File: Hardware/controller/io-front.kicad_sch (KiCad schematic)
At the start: 20 parts

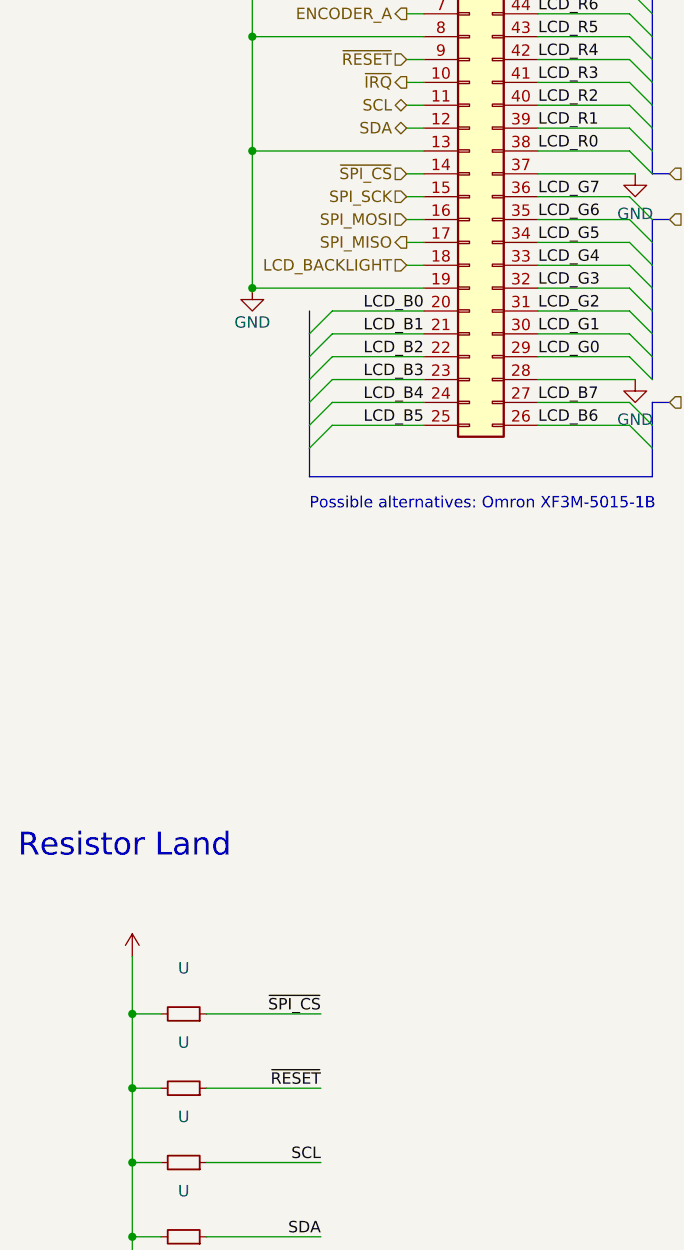
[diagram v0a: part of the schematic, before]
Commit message: hw: start working on rev4 controller
- removed SPI for display, and the associated SPI mux nonsense, and any
  superfluous resistors for pull-ups

- removed MAC address EEPROM

- start adding i2c RTC (which will also contain EEPROM with the MAC of
  the system, lol)

- start moving some components from bottom to top side of board

- tweaked positions of some mains voltage traces

- increased values of power indicator LED's current dropping resistors

- take 3V3 from SoM rather than generate it ourselves
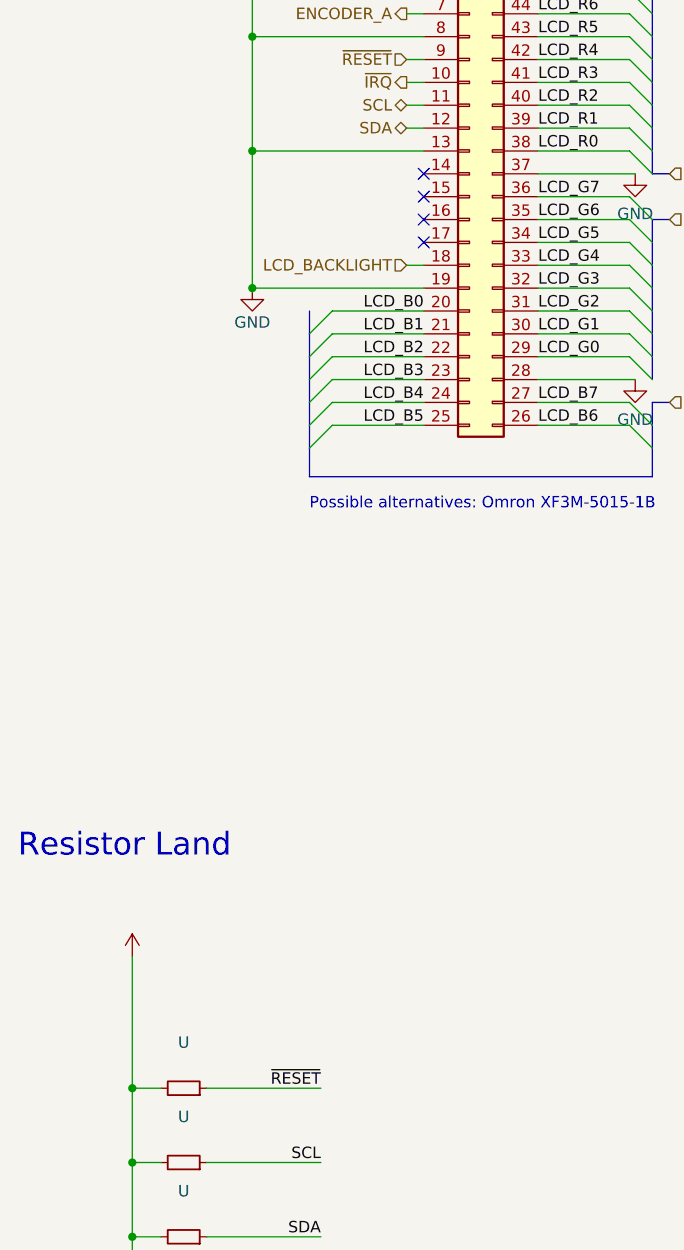
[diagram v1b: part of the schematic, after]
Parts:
- removed U: (no value), symbol Device:R_Small
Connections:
- net SPI_MISO: no longer names the net of J.17 (Pin_17)
- net SPI_MOSI: no longer names the net of J.16 (Pin_16)
- net SPI_SCK: no longer names the net of J.15 (Pin_15)
- net ~{SPI_CS}: no longer names the net of J.14 (Pin_14)
- no-connect marks 1 -> 5
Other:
- title: (none) -> Programmable Load Controller
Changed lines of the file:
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@@
 (kicad_sch (version 20220404) (generator eeschema)
   (paper "A4")
+  (title_block
+    (title "Programmable Load Controller")
+    (date "2022-06-28")
+    (rev "4")
+  )
   (junction (at 64.135 35.56) (diameter 0) (color 0 0 0 0)
   )
-  (junction (at 31.75 156.845) (diameter 0) (color 0 0 0 0)
-  )
   (junction (at 36.83 35.56) (diameter 0) (color 0 0 0 0)
   )
@@
   (junction (at 31.75 181.61) (diameter 0) (color 0 0 0 0)
   )
+  (no_connect (at 64.135 66.04))
   (no_connect (at 129.54 46.99))
+  (no_connect (at 64.135 68.58))
+  (no_connect (at 64.135 63.5))
+  (no_connect (at 64.135 71.12))
   (bus_entry (at 89.535 86.36) (size -2.54 -2.54)
     (stroke (width 0) (type default))
@@
     (stroke (width 0) (type default))
   )
-  (wire (pts (xy 62.23 71.12) (xy 64.135 71.12))
-    (stroke (width 0) (type default))
-  )
   (wire (pts (xy 62.23 50.8) (xy 64.135 50.8))
     (stroke (width 0) (type default))
@@
     (stroke (width 0) (type default))
   )
-  (wire (pts (xy 62.23 68.58) (xy 64.135 68.58))
-    (stroke (width 0) (type default))
-  )
   (wire (pts (xy 86.995 66.04) (xy 76.835 66.04))
     (stroke (width 0) (type default))
@@
     (stroke (width 0) (type default))
   )
-  (wire (pts (xy 40.005 156.845) (xy 52.705 156.845))
-    (stroke (width 0) (type default))
-  )
   (bus (pts (xy 89.535 63.5) (xy 91.44 63.5))
     (stroke (width 0) (type default))
@@
     (stroke (width 0) (type default))
   )
-  (wire (pts (xy 31.75 150.495) (xy 31.75 156.845))
-    (stroke (width 0) (type default))
-  )
   (bus (pts (xy 89.535 48.26) (xy 89.535 50.8))
     (stroke (width 0) (type default))
@@
     (stroke (width 0) (type default))
   )
-  (wire (pts (xy 31.75 156.845) (xy 31.75 165.1))
+  (wire (pts (xy 31.75 150.495) (xy 31.75 165.1))
     (stroke (width 0) (type default))
   )
@@
     (stroke (width 0) (type default))
   )
-  (wire (pts (xy 62.23 66.04) (xy 64.135 66.04))
-    (stroke (width 0) (type default))
-  )
   (wire (pts (xy 26.035 35.56) (xy 26.035 33.655))
     (stroke (width 0) (type default))
@@
     (stroke (width 0) (type default))
   )
-  (wire (pts (xy 62.23 63.5) (xy 64.135 63.5))
-    (stroke (width 0) (type default))
-  )
   (wire (pts (xy 184.15 36.83) (xy 185.42 36.83))
     (stroke (width 0) (type default))
@@
   )
   (wire (pts (xy 86.995 78.74) (xy 76.835 78.74))
-    (stroke (width 0) (type default))
-  )
-  (wire (pts (xy 31.75 156.845) (xy 34.925 156.845))
     (stroke (width 0) (type default))
   )
@@
     (effects (font (size 1.27 1.27)) (justify right bottom))
   )
-  (label "~{SPI_CS}" (at 52.705 156.845 0) (fields_autoplaced)
-    (effects (font (size 1.27 1.27)) (justify right bottom))
-  )
   (label "LCD_R6" (at 76.835 45.72 0) (fields_autoplaced)
     (effects (font (size 1.27 1.27)) (justify left bottom))
@@
     (effects (font (size 1.27 1.27)) (justify right))
   )
-  (hierarchical_label "SPI_SCK" (shape input) (at 62.23 66.04 180) (fields_autoplaced)
-    (effects (font (size 1.27 1.27)) (justify right))
-  )
   (hierarchical_label "ENCODER_A" (shape output) (at 62.23 45.72 180) (fields_autoplaced)
     (effects (font (size 1.27 1.27)) (justify right))
@@
     (effects (font (size 1.27 1.27)) (justify left))
   )
-  (hierarchical_label "SPI_MISO" (shape output) (at 62.23 71.12 180) (fields_autoplaced)
-    (effects (font (size 1.27 1.27)) (justify right))
-  )
   (hierarchical_label "LCD_R[0..7]" (shape input) (at 91.44 63.5 0) (fields_autoplaced)
     (effects (font (size 1.27 1.27)) (justify left))
@@
     (effects (font (size 1.27 1.27)) (justify left))
   )
-  (hierarchical_label "SPI_MOSI" (shape input) (at 62.23 68.58 180) (fields_autoplaced)
-    (effects (font (size 1.27 1.27)) (justify right))
-  )
   (hierarchical_label "LCD_B[0..7]" (shape input) (at 91.44 88.9 0) (fields_autoplaced)
     (effects (font (size 1.27 1.27)) (justify left))
-  )
-  (hierarchical_label "~{SPI_CS}" (shape input) (at 62.23 63.5 180) (fields_autoplaced)
-    (effects (font (size 1.27 1.27)) (justify right))
   )
   (hierarchical_label "SCL" (shape bidirectional) (at 62.23 55.88 180) (fields_autoplaced)
@@
       (effects (font (size 1.27 1.27)) hide)
     )
-    (pin "1")
-    (pin "2")
-  )
-  (symbol (lib_id "Device:R_Small") (at 37.465 156.845 270) (mirror x) (unit 1)
-    (in_bom yes) (on_board yes)
-    (default_instance (reference "U") (unit 1) (value "") (footprint ""))
-    (property "Reference" "U" (id 0) (at 37.465 151.765 90)
-      (effects (font (size 1.27 1.27)))
-    )
-    (property "Value" "" (id 1) (at 37.465 154.305 90)
-      (effects (font (size 1.27 1.27)))
-    )
-    (property "Footprint" "" (id 2) (at 37.465 156.845 0)
-      (effects (font (size 1.27 1.27)) hide)
-    )
-    (property "Datasheet" "~" (id 3) (at 37.465 156.845 0)
-      (effects (font (size 1.27 1.27)) hide)
-    )
-    (property "MPN" "" (id 4) (at 37.465 156.845 90)
-      (effects (font (size 1.27 1.27)) hide)
-    )

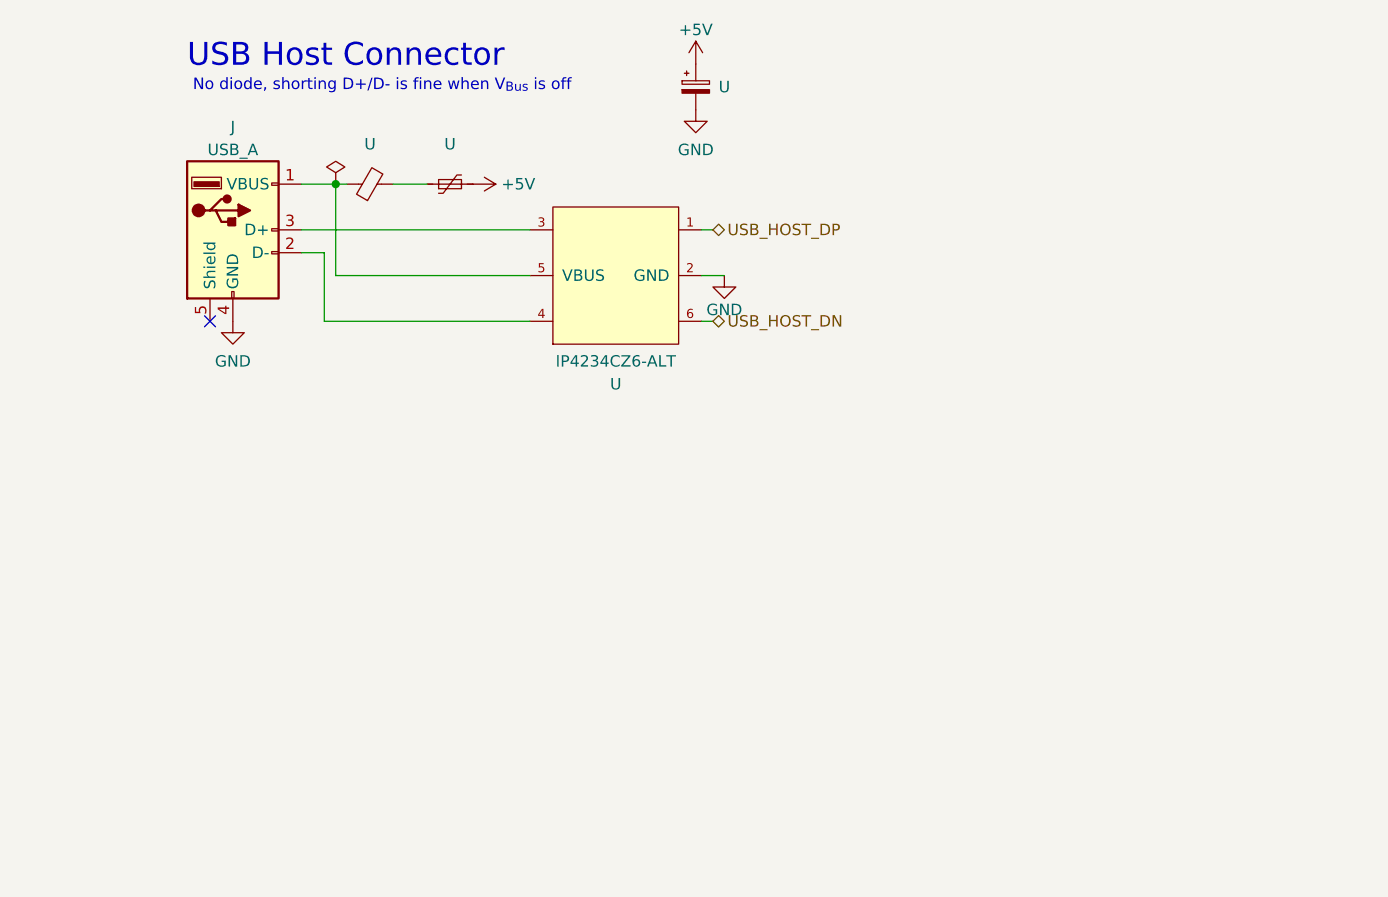
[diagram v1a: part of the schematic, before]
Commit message: hw: updates to usb host connector
- added a status indicator LED (including a lightpipe) next to the host
  connector

- start reworking the host connector power arrangement, using an actual
  USB power switch + current limiting IC (though we should revisit
  whether we'll use one without an error output)

- create footprint for AP22817 USB power switch
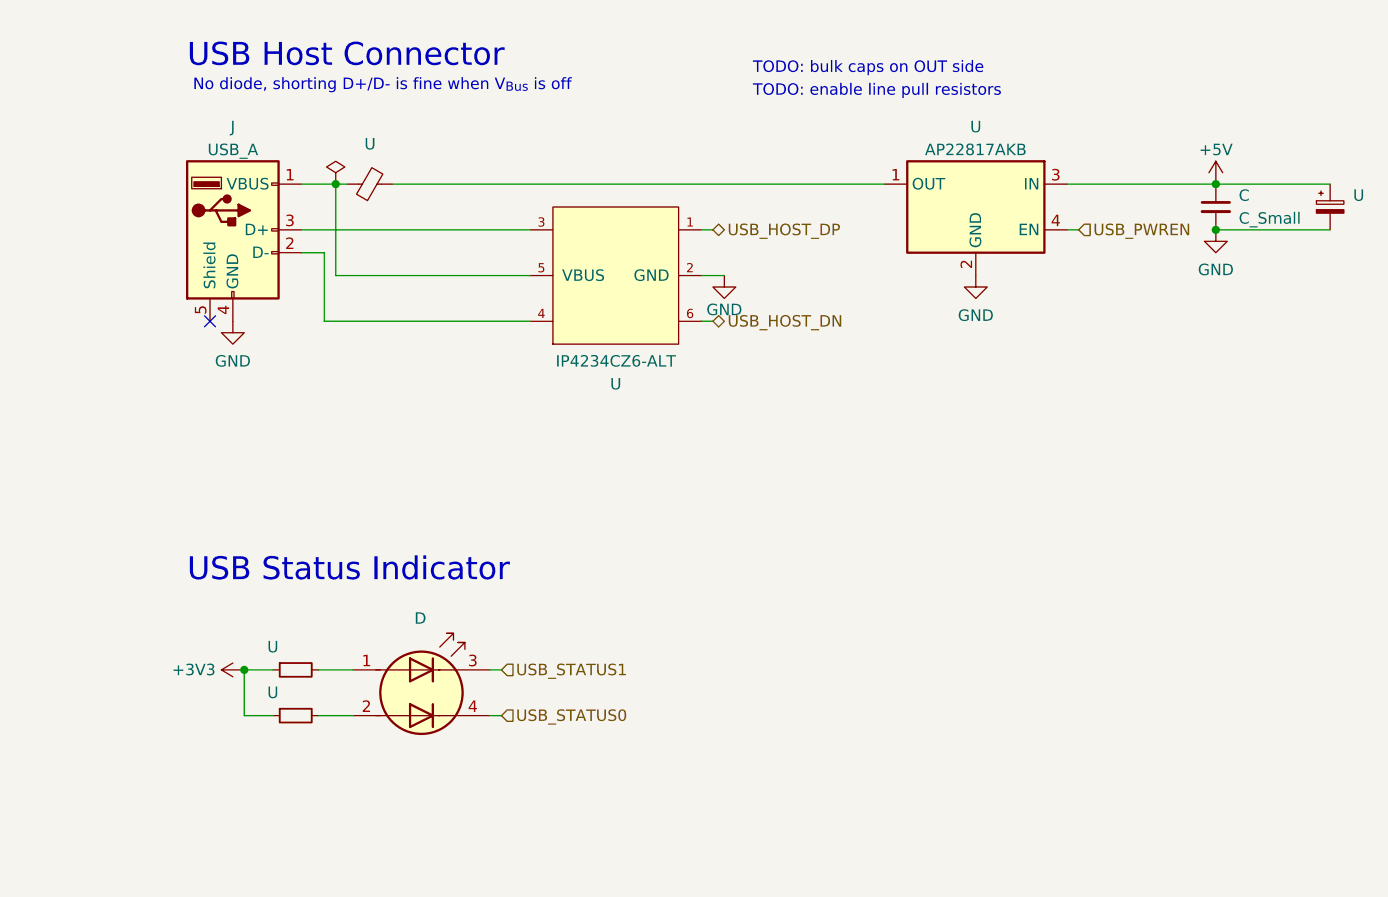
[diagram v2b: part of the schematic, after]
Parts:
- removed U: (no value), symbol Device:Polyfuse_Small
- added C: C_Small, symbol Device:C_Small
- added D: LED_Dual_AAKK, symbol Device:LED_Dual_AAKK
- added U (x2): (no value), symbol Device:R_Small
- added U: AP22817AKB, Package_SO:TSOP-5_1.65x3.05mm_P0.95mm, symbol programmable-load:AP22817AKB
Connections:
- net +3V3: now also U.1, U.1
- net +5V: now also C.1, U.3 (IN)
- net GND: now also C.2, U.2 (GND)
- net at U.2: now also U.1 (OUT), U.5 (OUT)
- new net: D.2 (A2), U.2
- new net: D.1 (A1), U.2
- new net USB_PWREN: U.4 (EN)
- new net USB_STATUS0: D.4 (K2)
- new net USB_STATUS1: D.3 (K1)
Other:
- note added: "TODO: bulk caps on OUT side"
- note added: "TODO: enable line pull resistors"
- note added: "USB Status Indicator"
- moved on the sheet: U

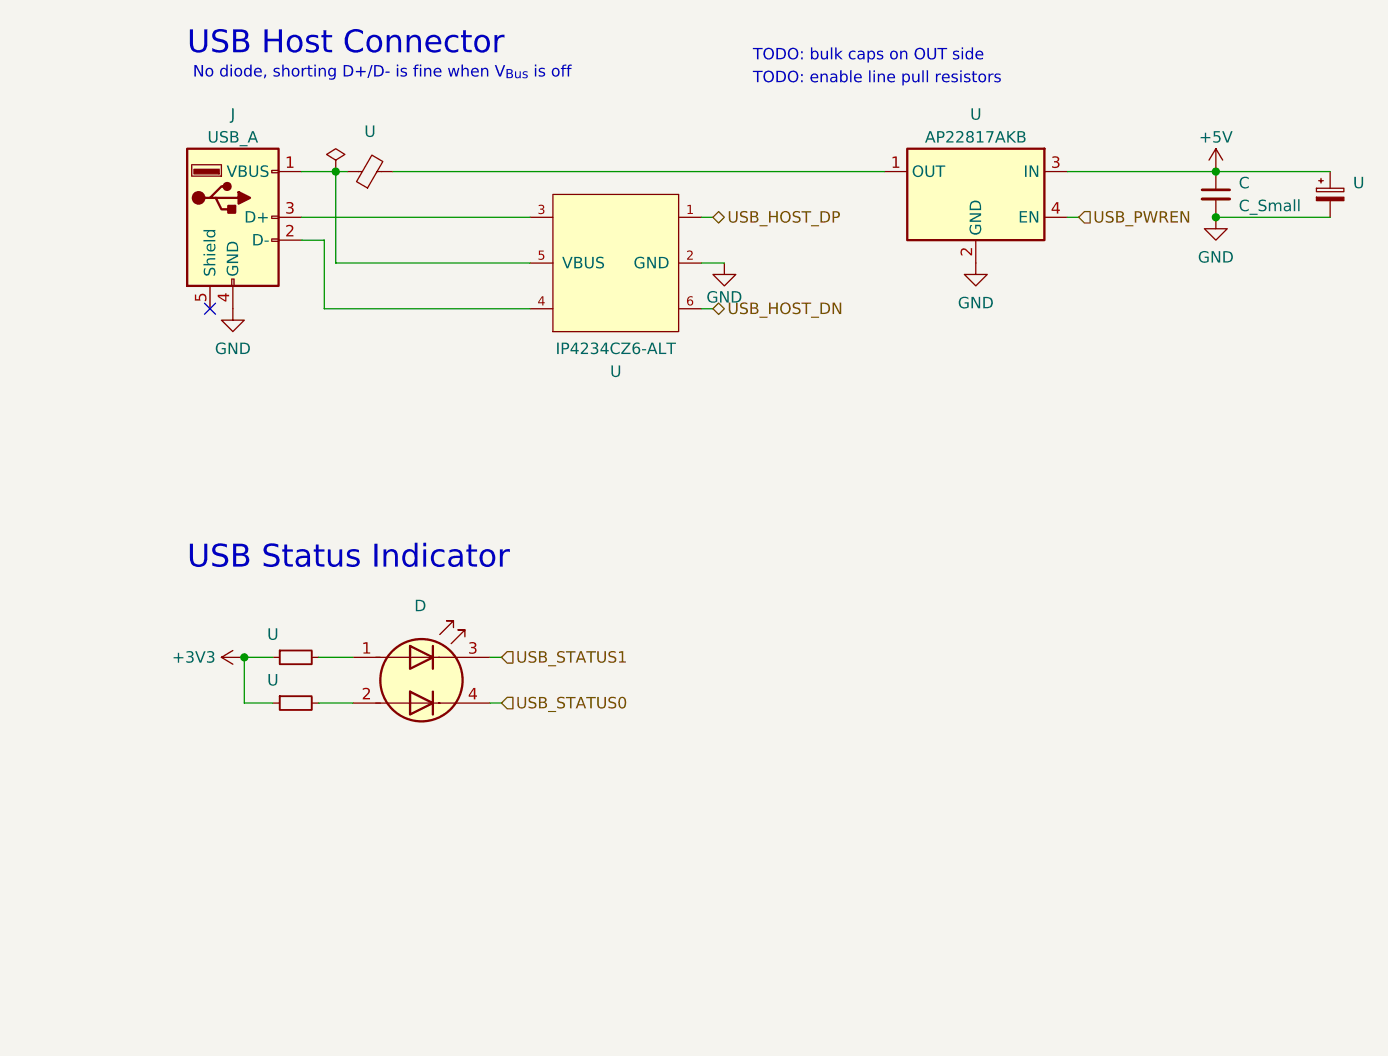
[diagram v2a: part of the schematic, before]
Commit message: hw: revise USB power stuff
- fixed the remaining usb powering stuff for the front panel host
  connector

- replaced 33µF SMD caps with through-hole equivalents

- removed some of the bottom mounted components for analog board power
  connection
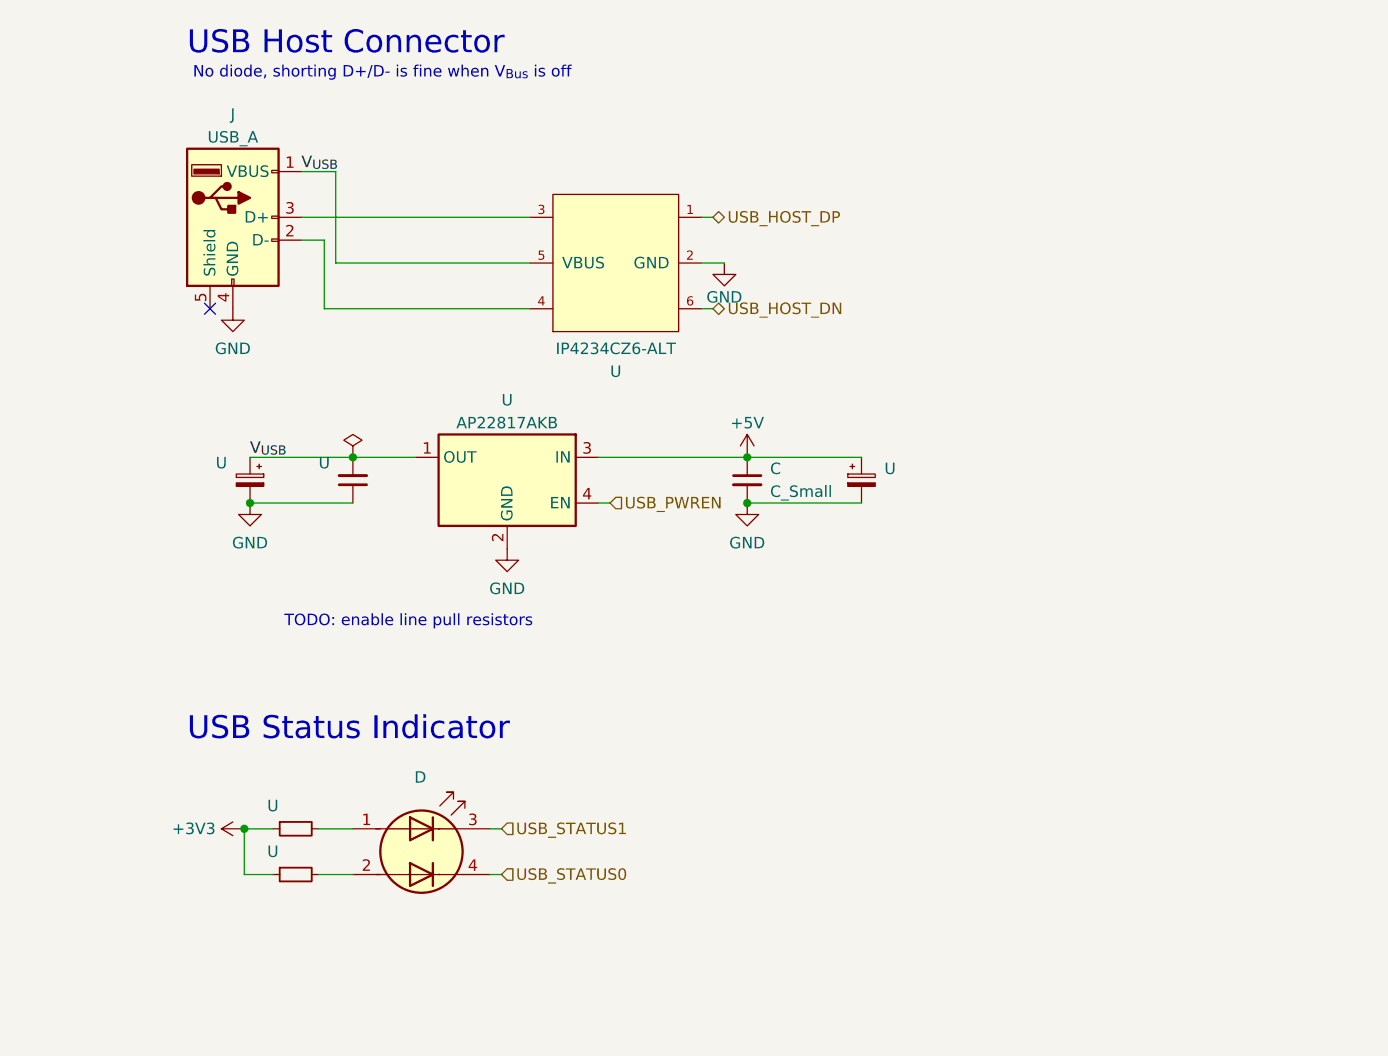
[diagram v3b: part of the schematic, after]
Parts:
- removed U: (no value), symbol Device:FerriteBead_Small
- removed U: (no value), symbol Device:C_Polarized_Small
- added U: (no value), symbol Device:C_Small
- added U (x2): (no value), symbol Device:C_Polarized_Small
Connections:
- net +5V: now also U.1
- net GND: now also U.1, U.2, U.2
- net V_{USB}: now reaches J.1 (VBUS), U.5 (VBUS)
- net V_{USB}: now also U.1 (OUT), U.5 (OUT), U.1, U.2
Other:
- note removed: "TODO: bulk caps on OUT side"
- moved on the sheet: C, D, U
